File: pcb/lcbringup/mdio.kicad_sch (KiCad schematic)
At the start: 14 parts, among them J2 CONN_01X10, U1 XC7A35T-2FGG484C, U3 ECS-1612MV-250-CN

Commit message: Continued line card bringup board
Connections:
- net ARTIX_LED_2: now also U1.AA21 (IO_L8N_T1_D12_14); no longer U1.AB20 (IO_L15N_T2_DQS_DOUT_CSO_B_14)
- net ARTIX_LED_3: now also U1.AB20 (IO_L15N_T2_DQS_DOUT_CSO_B_14); no longer U1.AB18 (IO_L17N_T2_A13_D29_14)
- net MDC: now also U1.W21 (IO_L7P_T1_D09_14); no longer U1.N14 (IO_L23N_T3_A02_D18_14)
- net MDIO: now also U1.Y21 (IO_L9P_T1_DQS_14); no longer U1.P16 (IO_L24P_T3_A01_D17_14)
- net SPI_CS_N: now also U1.R22 (IO_L1N_T0_D01_DIN_14); no longer U1.R14 (IO_L19N_T3_A09_D25_VREF_14)
- net SPI_MISO: now also U1.V22 (IO_L3N_T0_DQS_EMCCLK_14); no longer U1.T18 (IO_L20N_T3_A07_D23_14)
- net SPI_MOSI: now also U1.Y22 (IO_L9N_T1_DQS_D13_14); no longer U1.N17 (IO_L21P_T3_DQS_14)
- net SPI_SCK: now also U1.W22 (IO_L7N_T1_D10_14); no longer U1.R18 (IO_L20P_T3_A08_D24_14)
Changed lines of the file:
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@@
-	)
-	(no_connect
-		(at 104.14 41.91)
 	)
 	(no_connect
@@
 	)
 	(no_connect
+		(at 104.14 113.03)
+	)
+	(no_connect
 		(at 104.14 46.99)
 	)
@@
 	)
 	(no_connect
+		(at 104.14 146.05)
+	)
+	(no_connect
 		(at 104.14 151.13)
 	)
@@
 	)
 	(no_connect
-		(at 104.14 69.85)
-	)
-	(no_connect
 		(at 104.14 49.53)
 	)
@@
 	)
 	(no_connect
+		(at 104.14 123.19)
+	)
+	(no_connect
 		(at 104.14 120.65)
 	)
@@
 	)
 	(no_connect
-		(at 104.14 59.69)
-	)
-	(no_connect
-		(at 104.14 67.31)
-	)
-	(no_connect
 		(at 104.14 138.43)
 	)
 	(no_connect
-		(at 104.14 72.39)
+		(at 104.14 143.51)
 	)
 	(no_connect
@@
 	)
 	(no_connect
+		(at 104.14 125.73)
+	)
+	(no_connect
 		(at 104.14 133.35)
 	)
 	(no_connect
+		(at 104.14 130.81)
+	)
+	(no_connect
 		(at 104.14 118.11)
 	)
@@
 	)
 	(no_connect
-		(at 104.14 31.75)
-	)
-	(no_connect
-		(at 104.14 62.23)
+		(at 104.14 128.27)
 	)
 	(wire
@@
 	)
 	(label "MDC"
-		(at 104.14 143.51 180)
+		(at 104.14 59.69 180)
 		(fields_autoplaced yes)
 		(effects
@@
 	)
 	(label "ARTIX_LED_2"
-		(at 104.14 102.87 180)
+		(at 104.14 67.31 180)
 		(fields_autoplaced yes)
 		(effects
@@
 	)
 	(label "SPI_SCK"
-		(at 104.14 125.73 180)
+		(at 104.14 62.23 180)
 		(fields_autoplaced yes)
 		(effects
@@
 	)
 	(label "SPI_CS_N"
-		(at 104.14 123.19 180)
+		(at 104.14 31.75 180)
 		(fields_autoplaced yes)
 		(effects
@@
 	)
 	(label "SPI_MISO"
-		(at 104.14 128.27 180)
+		(at 104.14 41.91 180)
 		(fields_autoplaced yes)
 		(effects
@@
 	)
 	(label "ARTIX_LED_3"
-		(at 104.14 113.03 180)
+		(at 104.14 102.87 180)
 		(fields_autoplaced yes)
 		(effects
@@
 	)
 	(label "SPI_MOSI"
-		(at 104.14 130.81 180)
+		(at 104.14 72.39 180)
 		(fields_autoplaced yes)
 		(effects
@@
 	)
 	(label "MDIO"
-		(at 104.14 146.05 180)
-		(fields_autoplaced yes)
-		(effects
+		(at 104.14 69.85 180)
+		(fields_autoplaced yes)
+		(effects

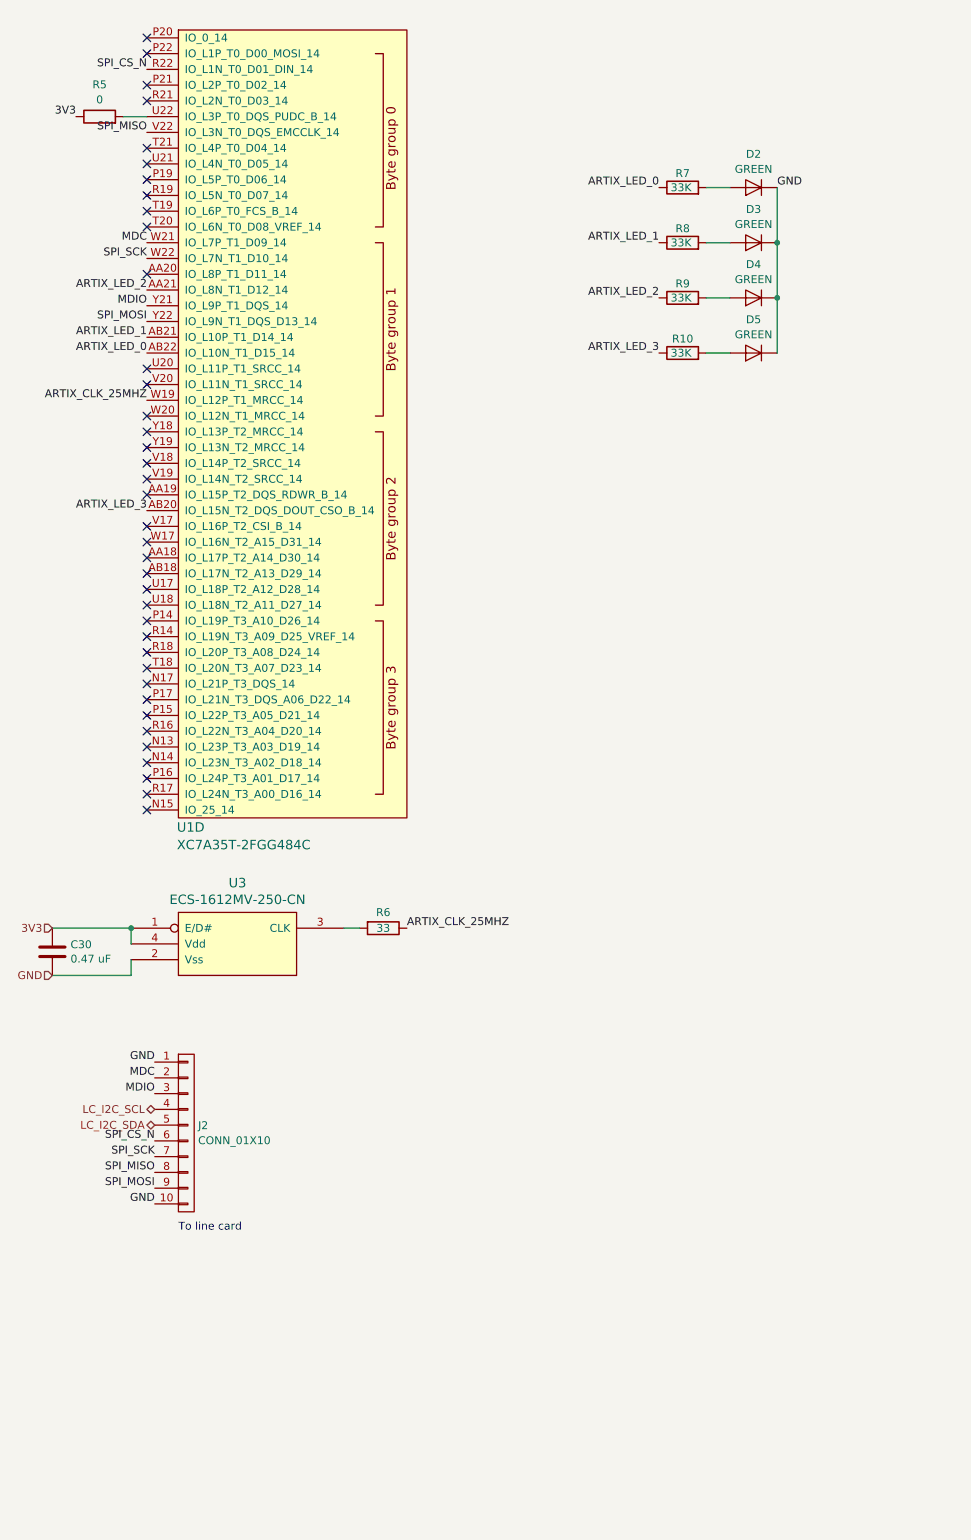
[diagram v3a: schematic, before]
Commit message: Conitnued lcbringup layout, power supply is now floorplanned
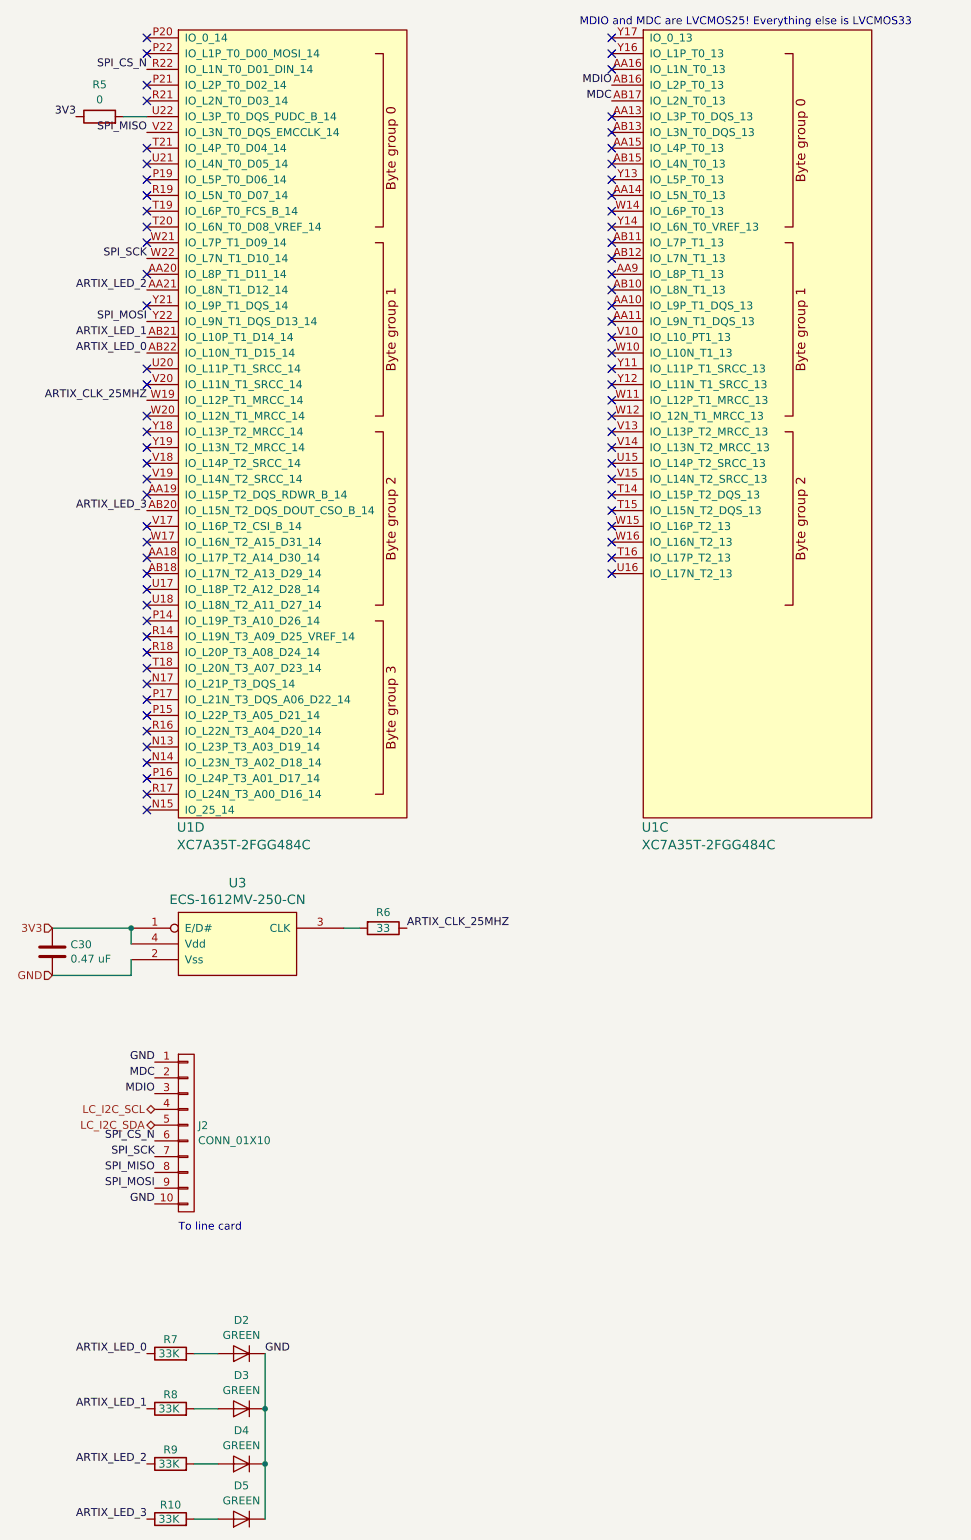
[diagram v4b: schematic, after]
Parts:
- added unit 3 of U1
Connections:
- net MDC: now also U1.AB17 (IO_L2N_T0_13); no longer U1.W21 (IO_L7P_T1_D09_14)
- net MDIO: now also U1.AB16 (IO_L2P_T0_13); no longer U1.Y21 (IO_L9P_T1_DQS_14)
- no-connect marks 38 -> 73
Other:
- note added: "MDIO and MDC are LVCMOS25! Everything else is LVCMOS33"
- moved on the sheet: D2, D3, D4, D5, R10, R7, R8, R9
